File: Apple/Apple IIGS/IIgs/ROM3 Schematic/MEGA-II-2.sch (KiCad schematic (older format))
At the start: 81 parts

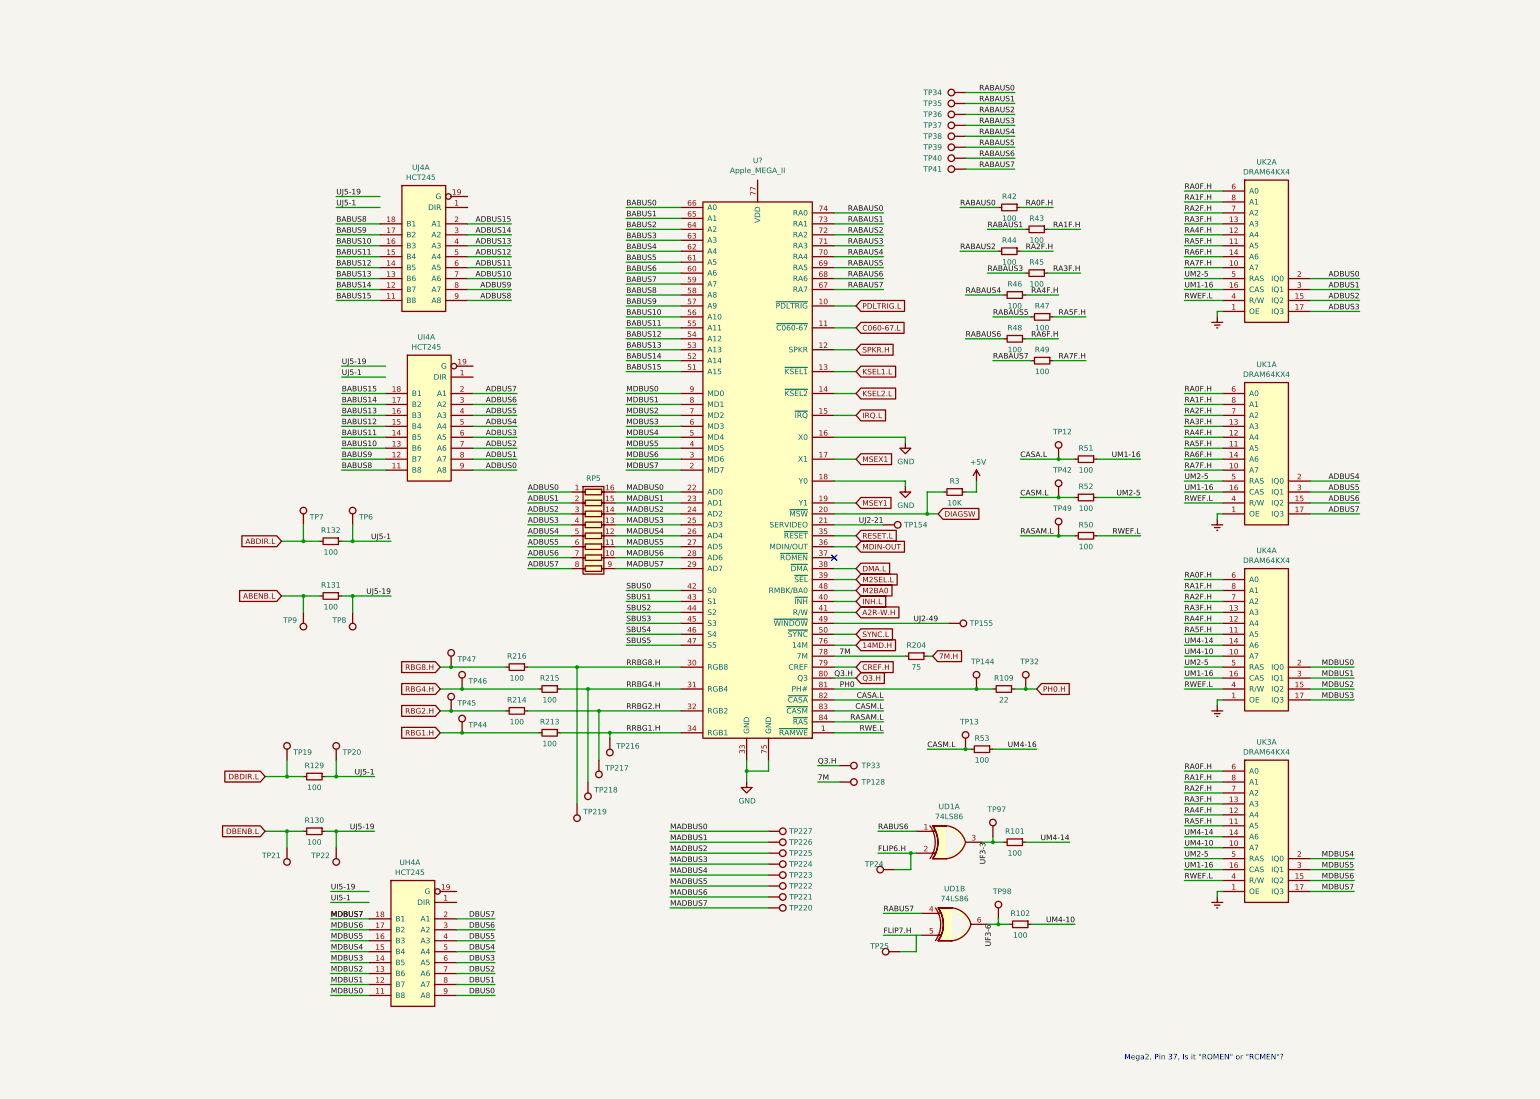
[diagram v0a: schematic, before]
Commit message: Clean-up after detailed circuit analysis - Fixed Reference to library in project file - Fixed BABUS tags on HCT245 (had wrong nets) - Flipped HCT245 circuits on MEGAII page to better match In/Out flow - Changed HCT245 symbol to move enable and DIR to better match In/Out Flow - Changed HCT245 into multi-unit symbol to put VCC/GND pins on Unit B - Fixed MEGAII designator - Fixed ADBUS nets on HCT245 (should be ABUS!) - Added notes with lessons learned from circuit deep-dive
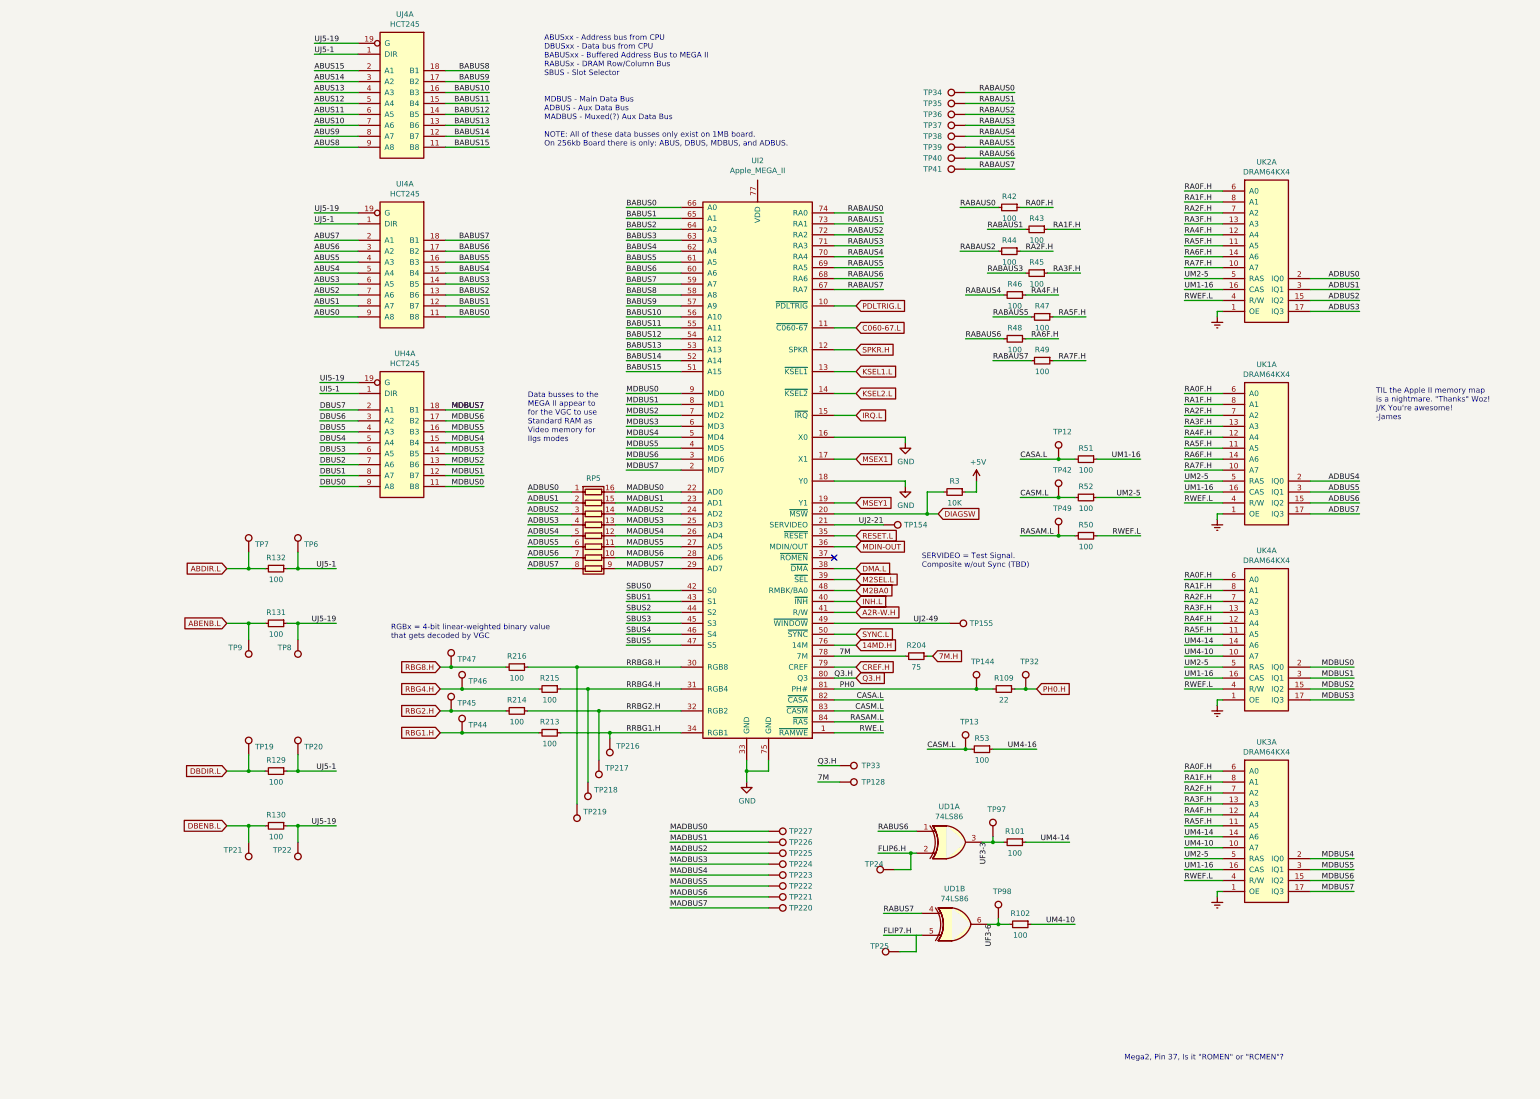
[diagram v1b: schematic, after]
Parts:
- gave numbers to parts that had none: 1
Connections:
- net ADBUS0: no longer UI4.9 (A8)
- net ADBUS1: no longer UI4.8 (A7)
- net ADBUS2: no longer UI4.7 (A6)
- net ADBUS3: no longer UI4.6 (A5)
- net ADBUS4: no longer UI4.5 (A4)
- net ADBUS5: no longer UI4.4 (A3)
- net ADBUS6: no longer UI4.3 (A2)
- net ADBUS7: no longer UI4.2 (A1)
- net BABUS0: now also UI4.11 (B8)
- net BABUS1: now also UI4.12 (B7)
- net BABUS10: no longer UI4.13 (B6)
- net BABUS11: no longer UI4.14 (B5)
- net BABUS12: no longer UI4.15 (B4)
- net BABUS13: no longer UI4.16 (B3)
- net BABUS14: no longer UI4.17 (B2)
- net BABUS15: no longer UI4.18 (B1)
- net BABUS2: now also UI4.13 (B6)
- net BABUS3: now also UI4.14 (B5)
- net BABUS4: now also UI4.15 (B4)
- net BABUS5: now also UI4.16 (B3)
- net BABUS6: now also UI4.17 (B2)
- net BABUS7: now also UI4.18 (B1)
- net BABUS8: no longer UI4.11 (B8)
- net BABUS9: no longer UI4.12 (B7)
- net UI5-1: now also UH4.1 (DIR)
- net UI5-19: now also UH4.19 (G)
- net UJ5-1: now also UI4.1 (DIR), UJ4.1 (DIR)
- net UJ5-19: now also UI4.19 (G), UJ4.19 (G)
- net ADBUS10 renamed ABUS10
- net ADBUS11 renamed ABUS11
- net ADBUS12 renamed ABUS12
- net ADBUS13 renamed ABUS13
- net ADBUS14 renamed ABUS14
- net ADBUS15 renamed ABUS15
- net ADBUS8 renamed ABUS8
- net ADBUS9 renamed ABUS9
- new net ABUS0: UI4.9 (A8)
- new net ABUS1: UI4.8 (A7)
- new net ABUS2: UI4.7 (A6)
- new net ABUS3: UI4.6 (A5)
- new net ABUS4: UI4.5 (A4)
- new net ABUS5: UI4.4 (A3)
- new net ABUS6: UI4.3 (A2)
- new net ABUS7: UI4.2 (A1)
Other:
- note added: "ABUSxx - Address bus from CPU\nDBUSxx - Data bus from CPU\nBABUSxx - Buffered Address Bus to MEGA II\nRABUSx - DRAM Row/Column Bus\nSBUS - Slot Selector\n\n\nMDBUS - Main Data Bus\nADBUS - Aux Data Bus\nMADBUS - Muxed(?) Aux Data Bus\n\nNOTE: All of these data busses only exist on 1MB board. \nOn 256kb Board there is only: ABUS, DBUS, MDBUS, and ADBUS."
- note added: "Data busses to the \nMEGA II appear to \nfor the VGC to use \nStandard RAM as \nVideo memory for \nIIgs modes"
- note added: "RGBx = 4-bit linear-weighted binary value \nthat gets decoded by VGC"
- note added: "SERVIDEO = Test Signal. \nComposite w/out Sync (TBD)\n"
- note added: "TIL the Apple II memory map \nis a nightmare. "Thanks" Woz!\nJ/K You're awesome!\n-James"
- moved on the sheet: R129, R130, R131, R132, TP19, TP20, TP21, TP22, TP6, TP7, TP8, TP9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

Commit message: started v2 updates on iigs-rom3
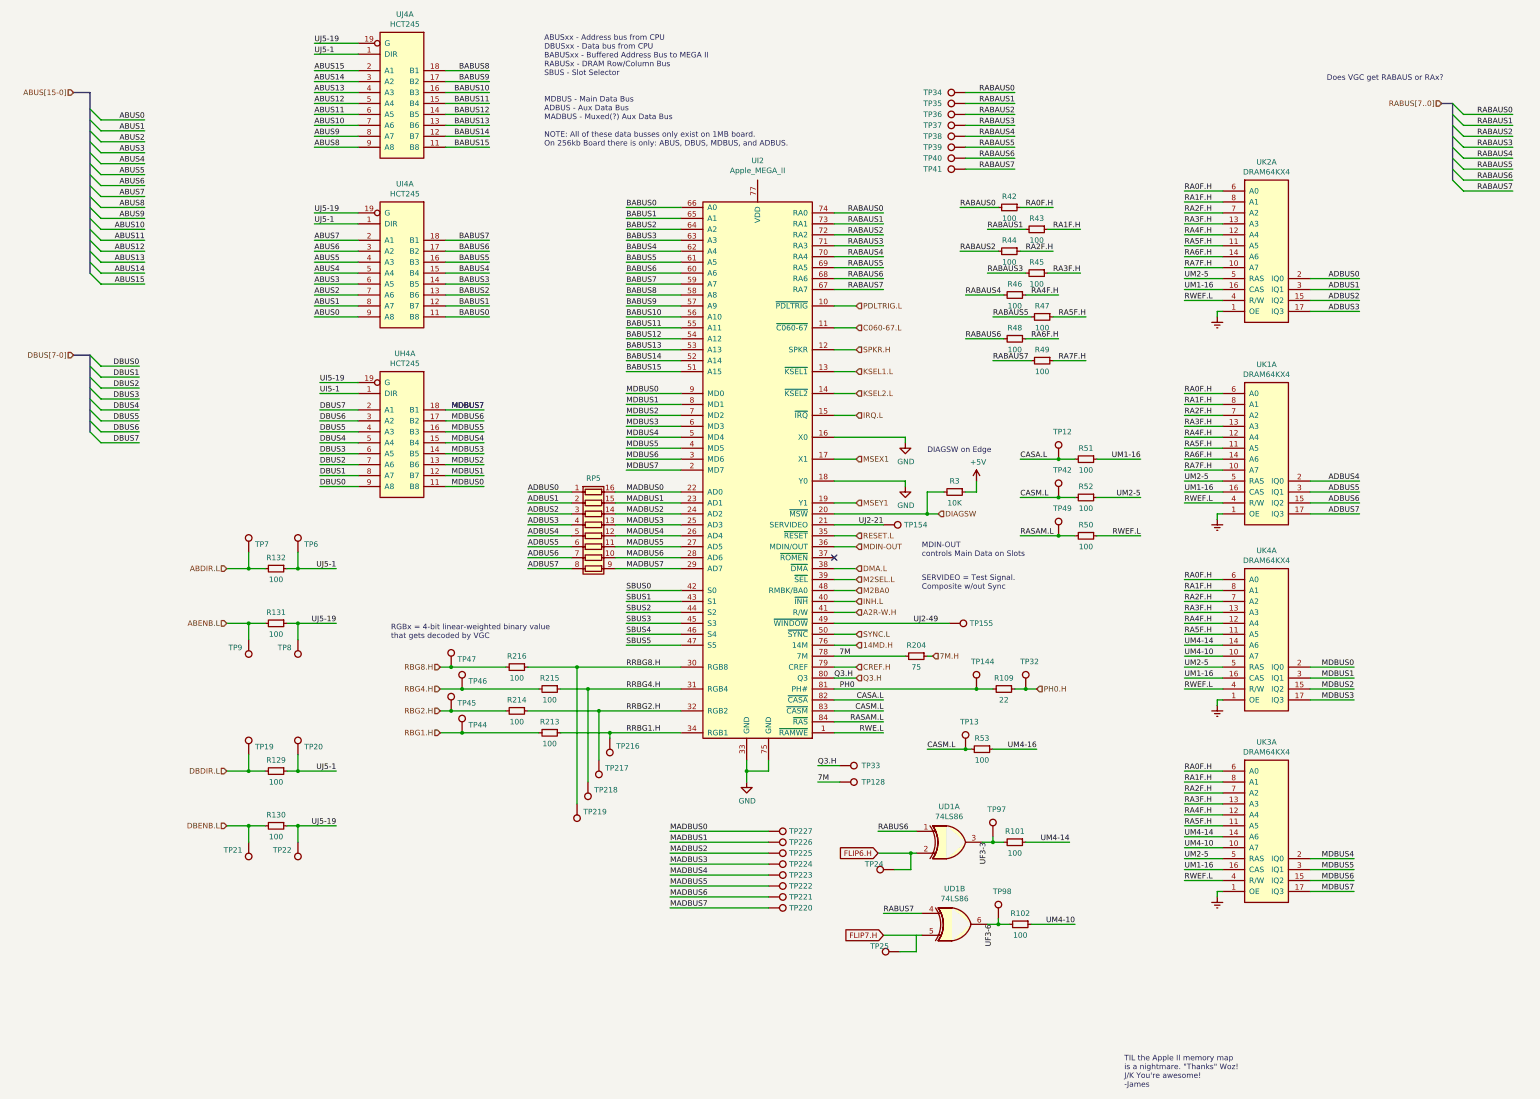
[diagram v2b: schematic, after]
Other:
- note added: "DIAGSW on Edge"
- note added: "Does VGC get RABAUS or RAx?"
- note added: "MDIN-OUT \ncontrols Main Data on Slots"
- note added: "SERVIDEO = Test Signal. \nComposite w/out Sync"
- note removed: "Data busses to the \nMEGA II appear to \nfor the VGC to use \nStandard RAM as \nVideo memory for \nIIgs modes"
- note removed: "Mega2, Pin 37, Is it "ROMEN" or "RCMEN"?"
- note removed: "SERVIDEO = Test Signal. \nComposite w/out Sync (TBD)\n"
